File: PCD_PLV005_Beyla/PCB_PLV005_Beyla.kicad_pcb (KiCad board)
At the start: 2 copper layers, 50 x 50 mm, 44 parts, among them J1 PWR/QB, J2 Switch_In, Q1 DMG2302UK-7, Q2 DMP2123L-7, U2 74HC266, U3 74HC08, U4 74HC21, U5 74LVC1G17, U6 LTC6993xS6-1

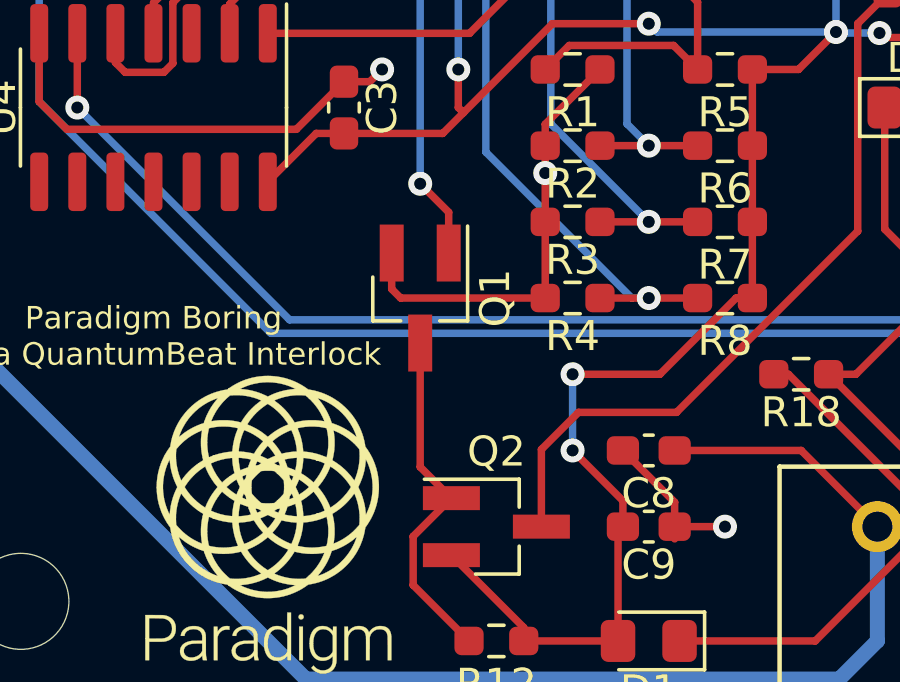
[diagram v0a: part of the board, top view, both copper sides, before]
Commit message: Fix Beyla footprint overlap
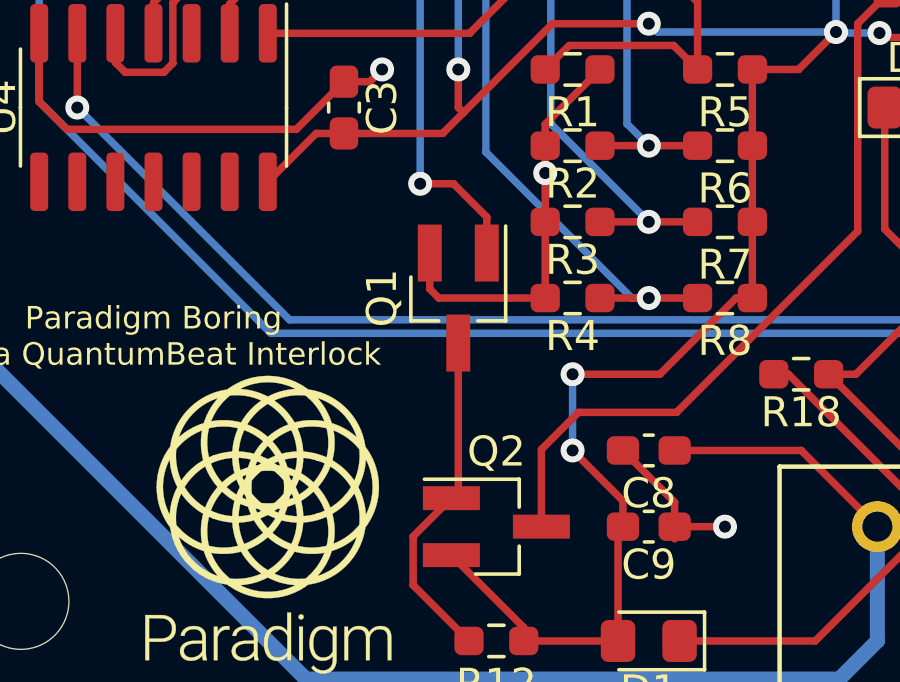
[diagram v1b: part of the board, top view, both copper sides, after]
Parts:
- moved Q1 1.27 mm to (68.6, 135.9)
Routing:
- net GND: track 120.6 -> 119.3 mm
- net Net-(Q1-Pad1): track 24.3 -> 25.4 mm

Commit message: Change power traces, clean up grounds on Beyla
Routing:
- net GND: track 119.3 -> 58.7 mm, vias 9 -> 15
